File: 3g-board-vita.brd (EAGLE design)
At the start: 30 x 26.8 mm, 2 parts

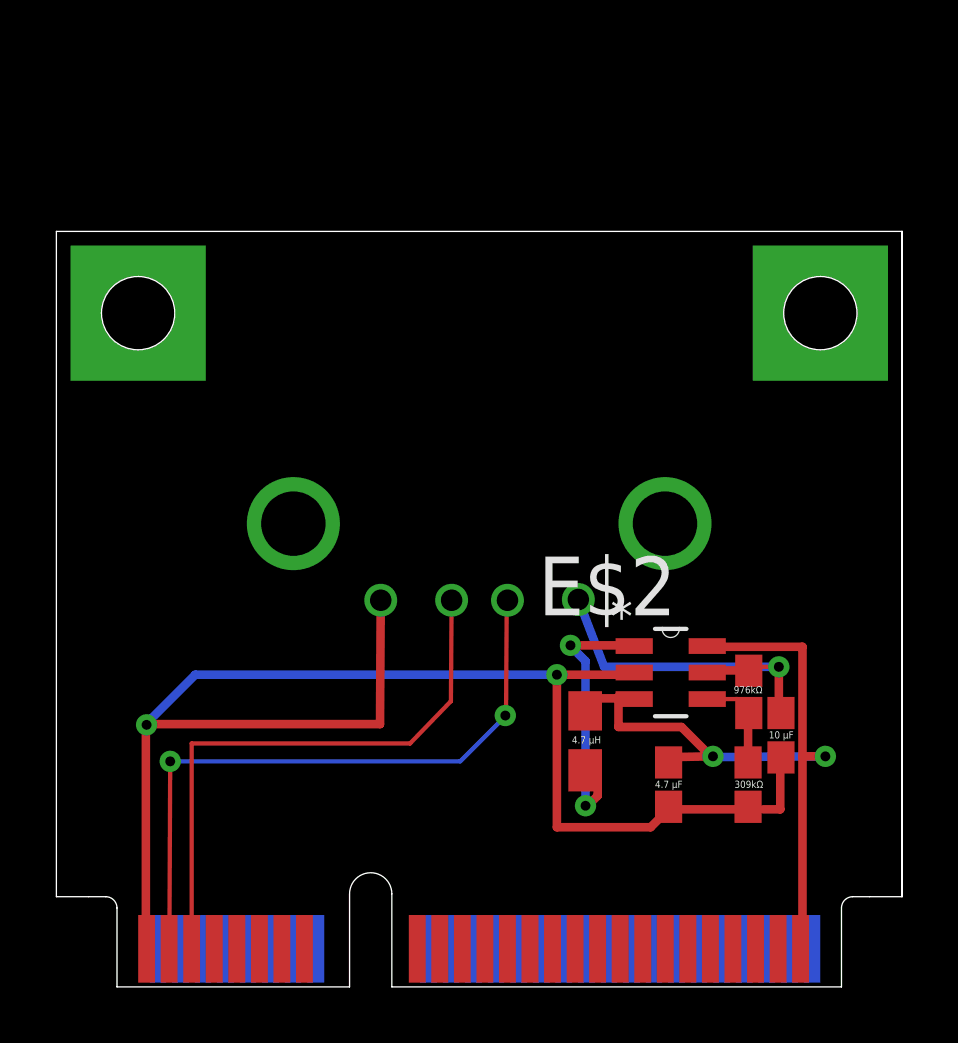
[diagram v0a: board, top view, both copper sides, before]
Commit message: Changed length and made own outside layer
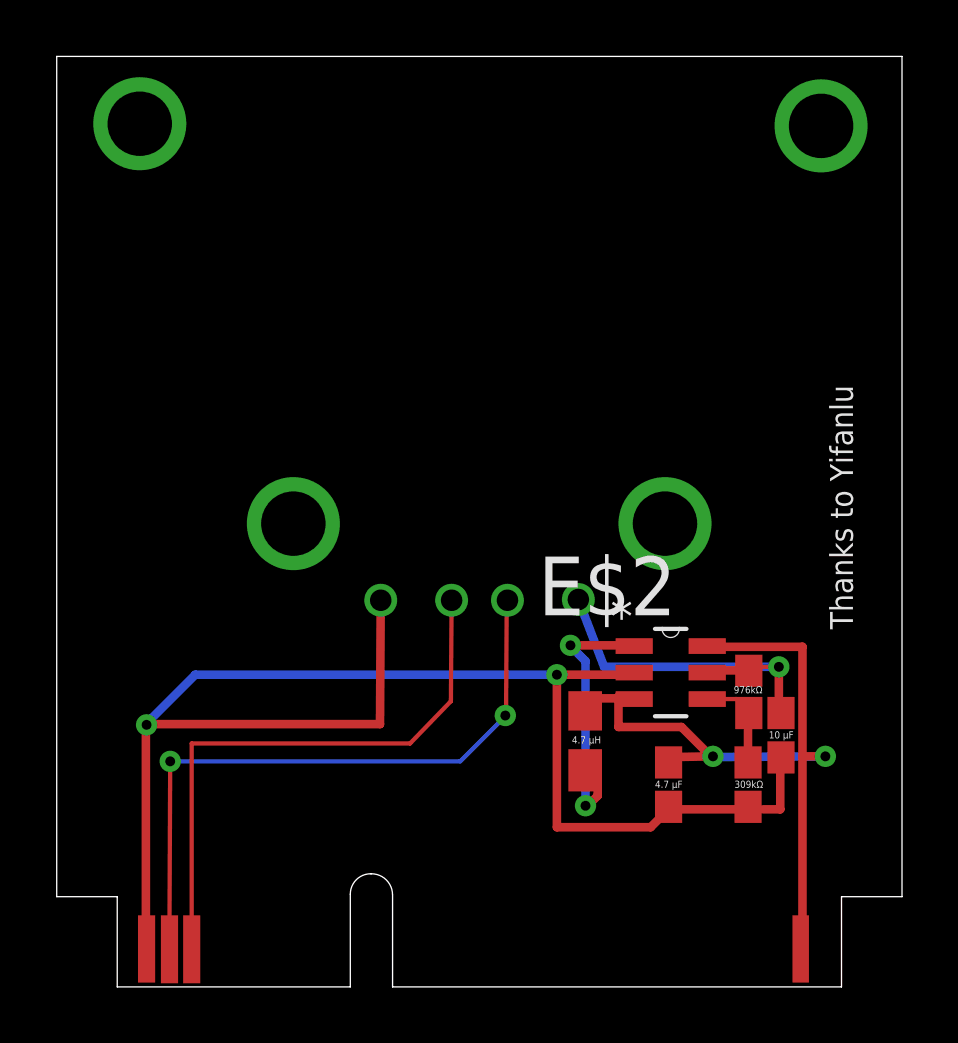
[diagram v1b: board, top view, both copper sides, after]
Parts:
- removed E$1: (no value), mini-pci-e:HALF-MINI-PCI-E
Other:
- board size 30 x 26.8 mm -> 30 x 33 mm
- board text added: "HaiHakkuIku VitaUSB v 3g-03"
- board text added: "Thanks to Yifanlu"
- board text removed: "HaiHakkuIku VitaUSB v 3g-02"
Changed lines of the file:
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@@
 <setting verticaltext="up"/>
 </settings>
-<grid distance="1" unitdist="mil" unit="mil" style="lines" multiple="1" display="yes" altdistance="5" altunitdist="mil" altunit="mil"/>
+<grid distance="0.5" unitdist="mil" unit="mil" style="lines" multiple="1" display="yes" altdistance="5" altunitdist="mil" altunit="mil"/>
 <layers>
 <layer number="1" name="Top" color="4" fill="1" visible="yes" active="yes"/>
+<layer number="2" name="Route2" color="1" fill="3" visible="yes" active="yes"/>
+<layer number="3" name="Route3" color="4" fill="3" visible="yes" active="yes"/>
+<layer number="4" name="Route4" color="1" fill="4" visible="yes" active="yes"/>
+<layer number="5" name="Route5" color="4" fill="4" visible="yes" active="yes"/>
+<layer number="6" name="Route6" color="1" fill="8" visible="yes" active="yes"/>
+<layer number="7" name="Route7" color="4" fill="8" visible="yes" active="yes"/>
+<layer number="8" name="Route8" color="1" fill="2" visible="yes" active="yes"/>
+<layer number="9" name="Route9" color="4" fill="2" visible="yes" active="yes"/>
+<layer number="10" name="Route10" color="1" fill="7" visible="yes" active="yes"/>
+<layer number="11" name="Route11" color="4" fill="7" visible="yes" active="yes"/>
+<layer number="12" name="Route12" color="1" fill="5" visible="yes" active="yes"/>
+<layer number="13" name="Route13" color="4" fill="5" visible="yes" active="yes"/>
+<layer number="14" name="Route14" color="1" fill="6" visible="yes" active="yes"/>
+<layer number="15" name="Route15" color="4" fill="6" visible="yes" active="yes"/>
 <layer number="16" name="Bottom" color="1" fill="1" visible="yes" active="yes"/>
 <layer number="17" name="Pads" color="2" fill="1" visible="yes" active="yes"/>
@@
 <rectangle x1="29.3116" y1="19.304" x2="30.2768" y2="20.447" layer="29"/>
 <rectangle x1="28.1686" y1="20.8026" x2="29.1338" y2="21.9456" layer="29"/>
-<text x="4.4196" y="21.7424" size="0.8128" layer="29">HaiHakkuIku
+<text x="4.445" y="21.5646" size="0.8128" layer="29">HaiHakkuIku
 VitaUSB
-v 3g-02</text>
+v 3g-03</text>
+<rectangle x1="6.985" y1="10.3124" x2="7.5946" y2="12.7" layer="1"/>
+<rectangle x1="7.7978" y1="10.287" x2="8.4074" y2="12.7" layer="1"/>
+<rectangle x1="8.5852" y1="10.287" x2="9.1948" y2="12.7" layer="1"/>
+<rectangle x1="30.2006" y1="10.3124" x2="30.7848" y2="12.7" layer="1"/>
+<wire x1="31.9405" y1="10.16" x2="31.9405" y2="13.3604" width="0.002540625" layer="20"/>
+<wire x1="6.2484" y1="13.3604" x2="6.2484" y2="10.16" width="0.002540625" layer="20"/>
+<wire x1="31.9405" y1="13.3604" x2="34.0868" y2="13.3604" width="0.002540625" layer="20"/>
+<wire x1="4.1021" y1="13.3604" x2="6.2484" y2="13.3604" width="0.002540625" layer="20"/>
+<wire x1="34.0868" y1="13.3604" x2="34.0868" y2="43.1673" width="0.002540625" layer="20"/>
+<rectangle x1="6.985" y1="10.3124" x2="7.5946" y2="12.7" layer="29"/>
+<rectangle x1="7.7978" y1="10.287" x2="8.4074" y2="12.7" layer="29"/>
+<rectangle x1="8.5852" y1="10.287" x2="9.1948" y2="12.7" layer="29"/>
+<rectangle x1="30.2006" y1="10.3124" x2="30.7848" y2="12.7" layer="29"/>
+<wire x1="14.5161" y1="10.16" x2="14.5161" y2="13.4493" width="0.002540625" layer="20"/>
+<wire x1="14.5161" y1="13.4493" x2="15.24" y2="14.1732" width="0.002540625" layer="20" curve="-90"/>
+<wire x1="15.24" y1="14.1732" x2="15.2654" y2="14.1732" width="0.002540625" layer="20"/>
+<wire x1="15.2654" y1="14.1732" x2="16.0147" y2="13.4239" width="0.002540625" layer="20" curve="-90"/>
+<wire x1="16.0147" y1="13.4239" x2="16.0147" y2="10.16" width="0.002540625" layer="20"/>
+<wire x1="4.1021" y1="43.1673" x2="4.1021" y2="13.3604" width="0.002540625" layer="20"/>
+<wire x1="34.0868" y1="43.1673" x2="4.1021" y2="43.1673" width="0.002540625" layer="20"/>
+<wire x1="6.2484" y1="10.16" x2="14.5161" y2="10.16" width="0.002540625" layer="20"/>
+<wire x1="31.9405" y1="10.16" x2="16.0147" y2="10.16" width="0.002540625" layer="20"/>
+<text x="32.3469" y="22.8473" size="0.8128" layer="121" rot="R90">Thanks to Yifanlu</text>
 </plain>
 <attributes>
@@
 </autorouter>
 <elements>
-<element name="E$1" library="mini-pci-e" package="HALF-MINI-PCI-E" value="" x="15.24" y="10.16"/>
 <element name="E$2" library="Microchip_By_element14_Batch_1" package="SOT95P270X145-6N" value="" x="25.8826" y="21.3106"/>
 </elements>
@@
 <signal name="S$2">
 <via x="12.4968" y="26.5938" extent="1-16" drill="2.286"/>
+<via x="7.0485" y="40.7797" extent="1-16" drill="2.286"/>
+<via x="31.2166" y="40.7035" extent="1-16" drill="2.286"/>
 </signal>
 <signal name="S$7">
